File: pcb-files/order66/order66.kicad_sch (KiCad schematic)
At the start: 212 parts, among them J1 NICEVIEW, J2 Pouch Battery Connector, J3 swd connector, J6 millmax connector, SW1 AUX1, SW10 Z, SW11 AUX7, SW12 2, SW13 W, SW14 S, SW15 X, SW16 LALT, SW17 3, SW18 E, SW19 D, SW2 ESC, SW20 C, SW21 GUI, SW22 4, SW23 R, SW24 F, SW25 V, SW26 RAISE, SW27 5, SW28 T, SW29 G, SW3 TAB, SW30 B, SW31 LSPACE, SW32 AUX2, SW33 6, SW34 Y, SW35 H, SW36 N, SW37 RSPACE, SW38 AUX3, SW39 7, SW4 CAPSLCK, SW40 U, SW41 J, SW42 M, SW43 LOWER, SW44 AUX4, SW45 8, SW46 I, SW47 K, SW48 ,<, SW49 LEFT, SW5 LSHIFT, SW50 9, SW51 O, SW52 L, SW53 .>, SW54 DOWN, SW55 AUX5, SW56 0, SW57 P, SW58 ;:, SW59 /?, SW6 LCTRL, SW60 UP, SW61 AUX6, SW62 BACKSPACE, SW63 BACKSLACH, SW64 ENTER, SW65 RSHIFT, SW66 RIGHT, SW67 RST, SW68 ON/OFF, SW7 1, SW8 Q, SW9 A, U1 NiceNano

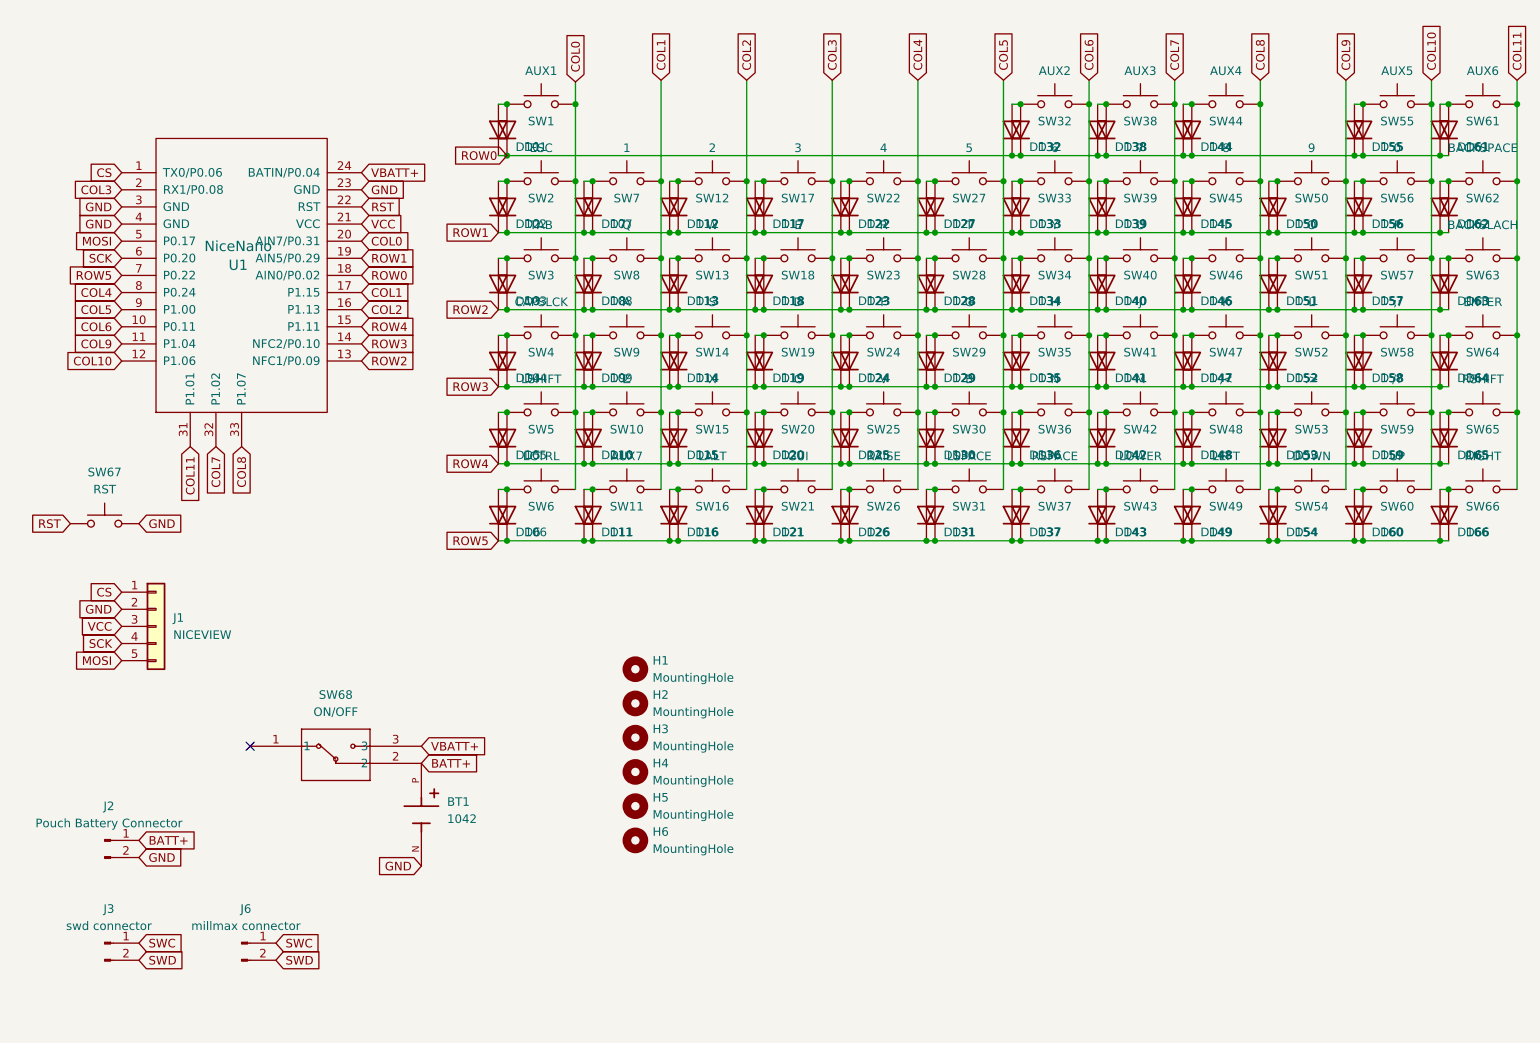
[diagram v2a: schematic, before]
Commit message: added the other version of power switch that I have as well just in case
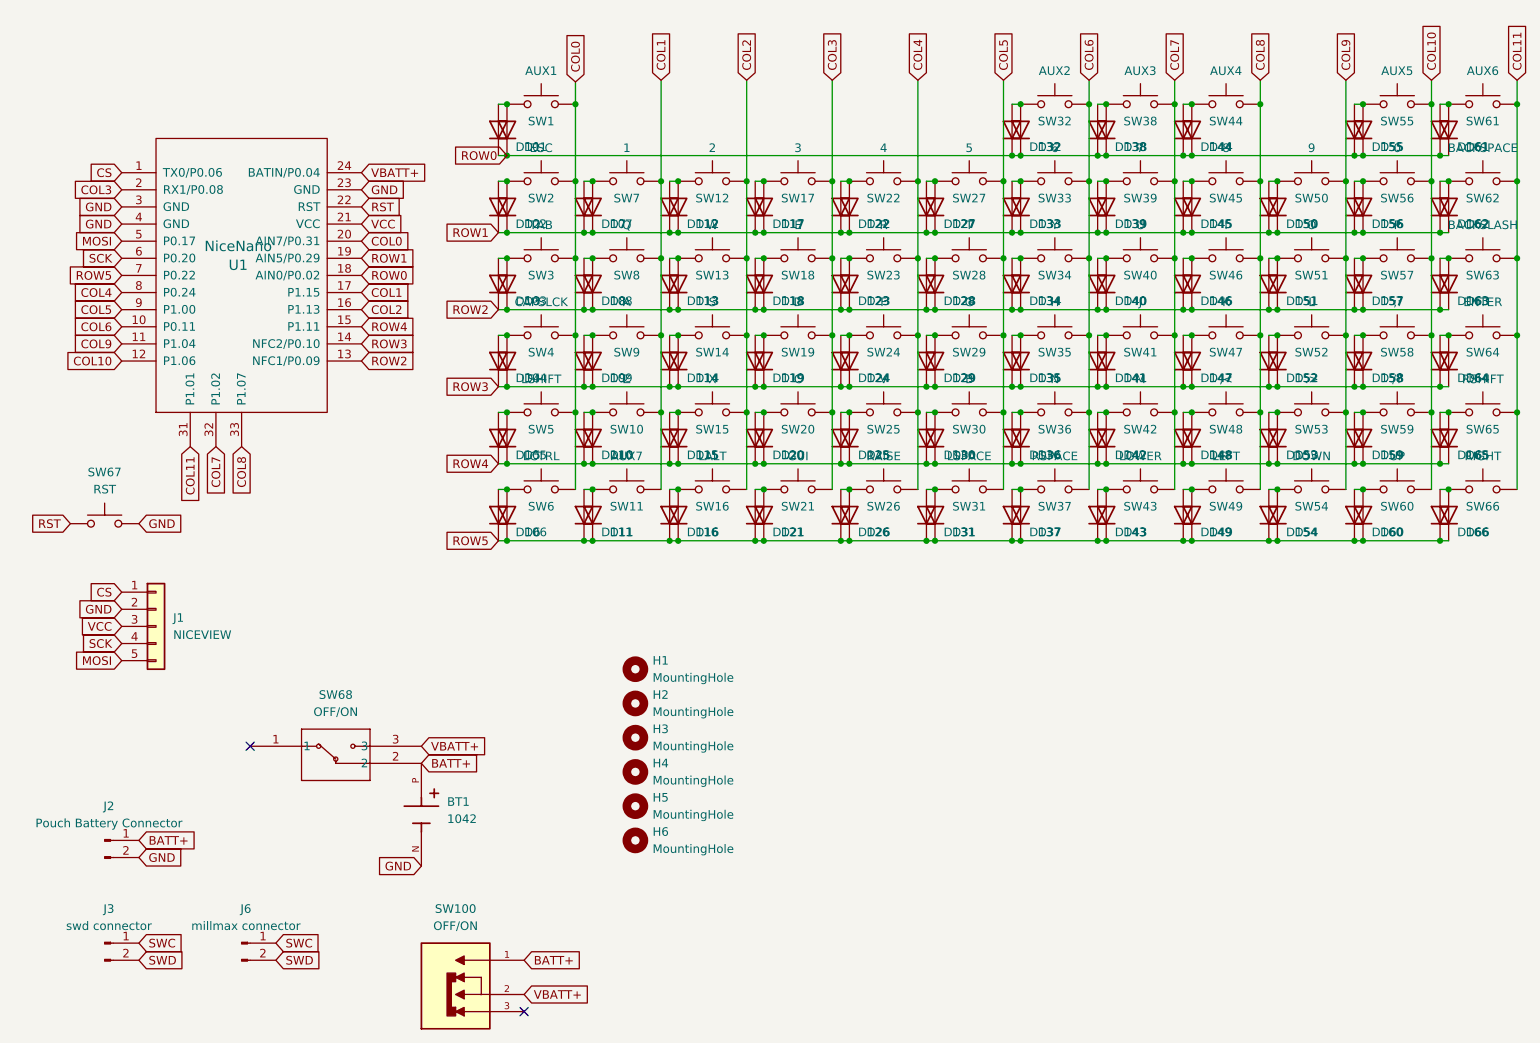
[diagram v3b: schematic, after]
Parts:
- added SW100: OFF/ON, SSSS811101:SW_SSSS811101, symbol SSSS811101:SSSS811101
- SW63: value BACKSLACH -> BACKSLASH
- SW68: value ON/OFF -> OFF/ON
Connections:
- net BATT+: now also SW100.1
- net VBATT+: now also SW100.2
- no-connect marks 1 -> 2
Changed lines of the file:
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@@
 		(at 55.88 144.78)
 	)
+	(no_connect
+		(at 96.52 184.15)
+	)
 	(wire
 		(pts
@@
 		)
 	)
+	(global_label "VBATT+"
+		(shape input)
+		(at 96.52 181.61 0)
+		(fields_autoplaced yes)
+		(effects
+			(font
+				(size 1.27 1.27)
+			)
+			(justify left)
+		)
+		(property "Intersheetrefs" "${INTERSHEET_REFS}"
+			(at 106.46 181.61 0)
+			(effects
+				(font
+					(size 1.27 1.27)
+				)
+				(justify left)
+				(hide yes)
+			)
+		)
+	)
 	(global_label "RST"
 		(shape input)
@@
 		)
 	)
+	(global_label "VBATT+"
+		(shape input)
+		(at 81.28 144.78 0)
+		(fields_autoplaced yes)
+		(effects
+			(font
+				(size 1.27 1.27)
+			)
+			(justify left)
+		)
+		(property "Intersheetrefs" "${INTERSHEET_REFS}"
+			(at 91.22 144.78 0)
+			(effects
+				(font
+					(size 1.27 1.27)
+				)
+				(justify left)
+				(hide yes)
+			)
+		)
+	)
 	(global_label "VCC"
 		(shape input)
@@
 		)
 	)
+	(global_label "BATT+"
+		(shape input)
+		(at 96.52 176.53 0)
+		(fields_autoplaced yes)
+		(effects
+			(font
+				(size 1.27 1.27)
+			)
+			(justify left)
+		)
+		(property "Intersheetrefs" "${INTERSHEET_REFS}"
+			(at 105.3714 176.53 0)
+			(effects
+				(font
+					(size 1.27 1.27)
+				)
+				(justify left)
+				(hide yes)
+			)
+		)
+	)
 	(global_label "SWC"
 		(shape input)
@@
 		)
 	)
-	(global_label "VBATT+"
-		(shape input)
-		(at 81.28 144.78 0)
-		(fields_autoplaced yes)
-		(effects
-			(font
-				(size 1.27 1.27)
-			)
-			(justify left)
-		)
-		(property "Intersheetrefs" "${INTERSHEET_REFS}"
-			(at 91.22 144.78 0)
-			(effects
-				(font
-					(size 1.27 1.27)
-				)
-				(justify left)
-				(hide yes)
-			)
-		)
-	)
 	(global_label "BATT+"
 		(shape input)
@@
 	)
 	(symbol
+		(lib_id "SSSS811101:SSSS811101")
+		(at 86.36 179.07 0)
+		(unit 1)
+		(exclude_from_sim no)
+		(in_bom yes)
+		(on_board yes)
+		(dnp no)
+		(fields_autoplaced yes)
+		(property "Reference" "SW100"
+			(at 86.36 168.91 0)
+			(effects
+				(font
+					(size 1.27 1.27)
+				)
+			)
+		)
+		(property "Value" "OFF/ON"
+			(at 86.36 171.45 0)
+			(effects
+				(font
+					(size 1.27 1.27)
+				)
+			)
+		)
+		(property "Footprint" "SSSS811101:SW_SSSS811101"
+			(at 86.36 179.07 0)
+			(effects
+				(font
+					(size 1.27 1.27)
+				)
+				(justify bottom)
+				(hide yes)
+			)
+		)
+		(property "Datasheet" ""
+			(at 86.36 179.07 0)
+			(effects
+				(font
+					(size 1.27 1.27)
+				)
+				(hide yes)
+			)
+		)
+		(property "Description" ""
+			(at 86.36 179.07 0)
+			(effects
+				(font
+					(size 1.27 1.27)
+				)
+				(hide yes)
+			)
+		)
+		(property "PARTREV" "N/A"
+			(at 86.36 179.07 0)
+			(effects
+				(font
+					(size 1.27 1.27)
+				)
+				(justify bottom)
+				(hide yes)
+			)
+		)
+		(property "STANDARD" "Manufacturer Recommendations"
+			(at 86.36 179.07 0)
+			(effects
+				(font
+					(size 1.27 1.27)
+				)
+				(justify bottom)
+				(hide yes)
+			)
+		)
+		(property "MAXIMUM_PACKAGE_HEIGHT" "1.60 mm"
+			(at 86.36 179.07 0)
+			(effects
+				(font
+					(size 1.27 1.27)
+				)
+				(justify bottom)
+				(hide yes)
+			)
+		)
+		(property "MANUFACTURER" "ALPS"
+			(at 86.36 179.07 0)
+			(effects
+				(font
+					(size 1.27 1.27)
+				)
+				(justify bottom)
+				(hide yes)
+			)
+		)
+		(pin "3"
+		)
+		(pin "1"
+		)
+		(pin "2"
+		)
+		(instances
+			(project ""
+				(path "/4342f055-467b-4789-a8ed-b19f1b214d4d"
+					(reference "SW100")
+					(unit 1)
+				)
+			)
+		)
+	)
+	(symbol
 		(lib_id "Switch:SW_Push")
 		(at 187.96 95.25 0)
@@
 			)
 		)
-		(property "Value" "ON/OFF"
+		(property "Value" "OFF/ON"
 			(at 68.58 139.7 0)
 			(effects
@@
 			)
 		)
-		(property "Value" "BACKSLACH"
+		(property "Value" "BACKSLASH"
 			(at 238.76 67.4624 0)
 			(effects
